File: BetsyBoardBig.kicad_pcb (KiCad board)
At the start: 4 copper layers, 50 x 50 mm, 55 parts, among them J1 USB_B_Micro, J2 Micro_SD_Card, J3 CLOCKS, J4 USART3, J5 SPI/USART, J6 I2C, J7 ANALOG, P3 CORTEX-JTAG, P6 BATT, Q1 BSS138BKS, SW1 JUMPER_x2, SW2 RST, SW3 USR, U1 TLV75733PDBVR‎, U2 USBLC6-2SC6, U3 APX823, U4 STM32L486Rx-LQFP64, U5 IS25WP256D-xM, U6 74LVC1G3157, X1 XTAL, Y1 Crystal

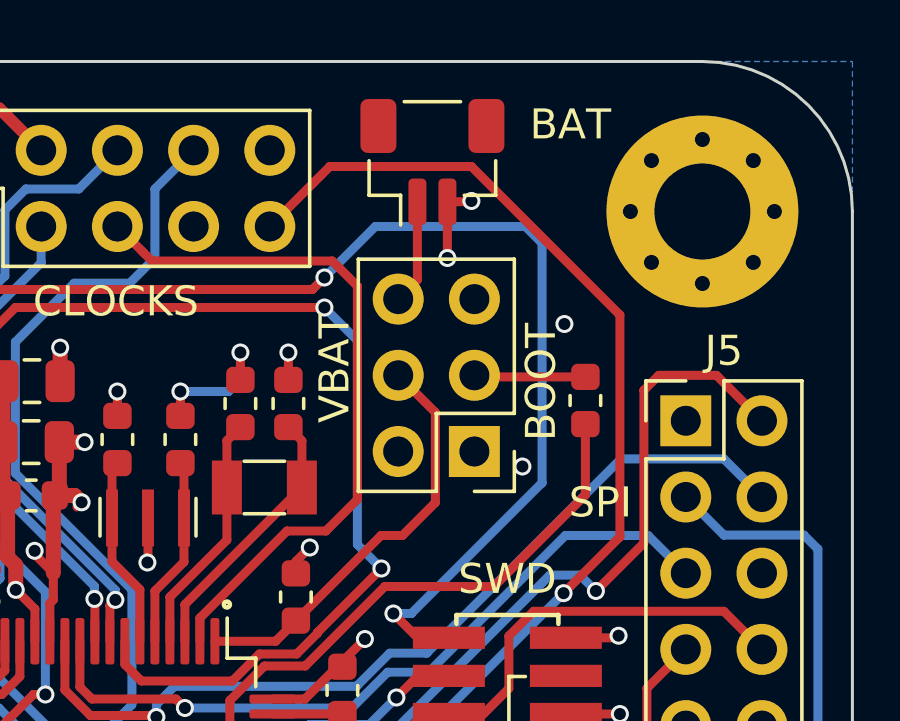
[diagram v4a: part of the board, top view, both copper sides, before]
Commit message: Use a battery header I can actually procure.
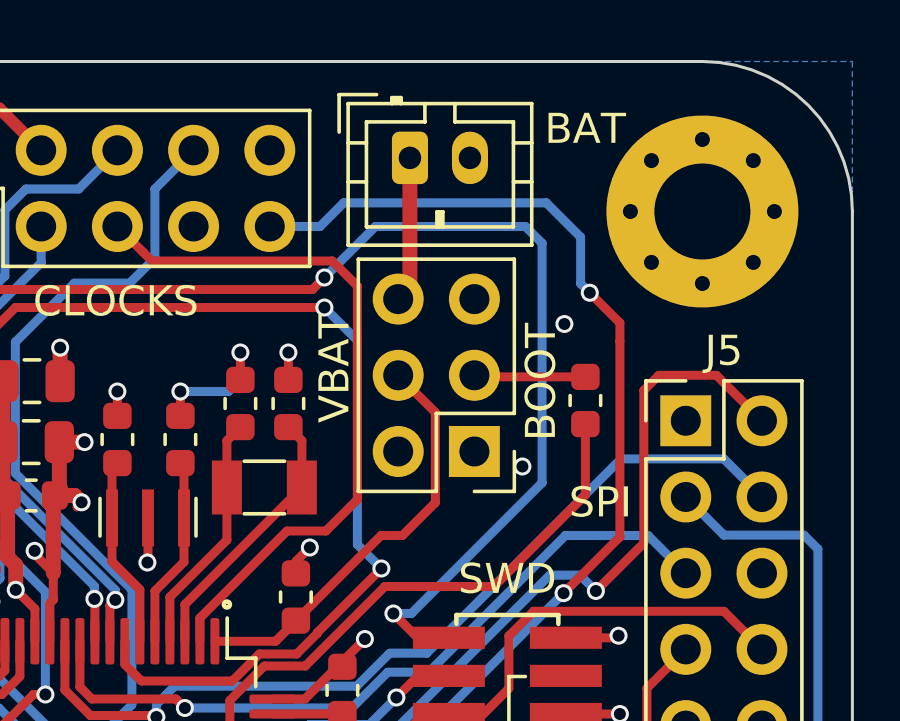
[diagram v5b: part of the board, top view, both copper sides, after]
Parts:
- P6: footprint Connector_JST:JST_SH_BM02B-SRSS-TB_1x02-1MP_P1.00mm_Vertical -> Connector_JST:JST_PH_B2B-PH-K_1x02_P2.00mm_Vertical
- moved P6 0.76 mm to (130.3, 53.2)
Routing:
- net GND: track 93.2 -> 90.5 mm, vias 48 -> 46
- net /VBAT_IN: track 3.51 -> 4.87 mm
- net /SWCLK_JTCK: track 43.3 -> 43.0 mm, vias 3 -> 4

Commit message: Simplify a bit.
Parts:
- J3: footprint Connector_PinHeader_2.54mm:PinHeader_2x05_P2.54mm_Vertical -> Connector_PinHeader_2.54mm:PinHeader_2x04_P2.54mm_Vertical
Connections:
- J3 pad 2: /EXTSCL -> /OCLK_LS
- J3 pad 3: /RTC_OUT -> /EXTSCL
- J3 pad 4: /EXTSDA -> /OCLK_M
- J3 pad 5: /RTC_TS -> /EXTSDA
- J3 pad 6: /OCLK_LS -> /RTC_OUT
- J3 pad 7: (no net) -> GND
- J3 pad 8: /OCLK_M -> /RTC_TS
- J5 pad 7: /SWDIO_JTMS -> (no net)
- J5 pad 8: /SWO_JTDO -> (no net)
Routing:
- net /SWCLK_JTCK: track 43.0 -> 19.5 mm, vias 4 -> 3
- net /SWDIO_JTMS: track 28.6 -> 12.1 mm
- net /SWO_JTDO: track 21.3 -> 7.92 mm
- net /QSPI_IO3: track 26.7 -> 14.2 mm
- net /RTC_OUT: track 29.4 -> 39.2 mm
- net /SDMMC_CLK: track 30.4 -> 20.7 mm, vias 0 -> 2
- net /SDMMC_D2: track 30.6 -> 21.9 mm
- net /SDMMC_CMD: track 30.5 -> 23.0 mm, vias 0 -> 2
- net /SDMMC_D3: track 30.4 -> 23.0 mm
- net VCC: track 70.4 -> 75.1 mm, vias 23 -> 22
- net /LED_RED: track 23.5 -> 20.2 mm
- net /OCLK_M: track 35.5 -> 32.7 mm
- net /USR_BTN: track 35.6 -> 33.1 mm
- net /OCLK_LS: track 22.6 -> 20.6 mm
- net /USART3_TXD: track 26.4 -> 24.5 mm
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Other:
- board text added: "JLCJLCJLCJLC"

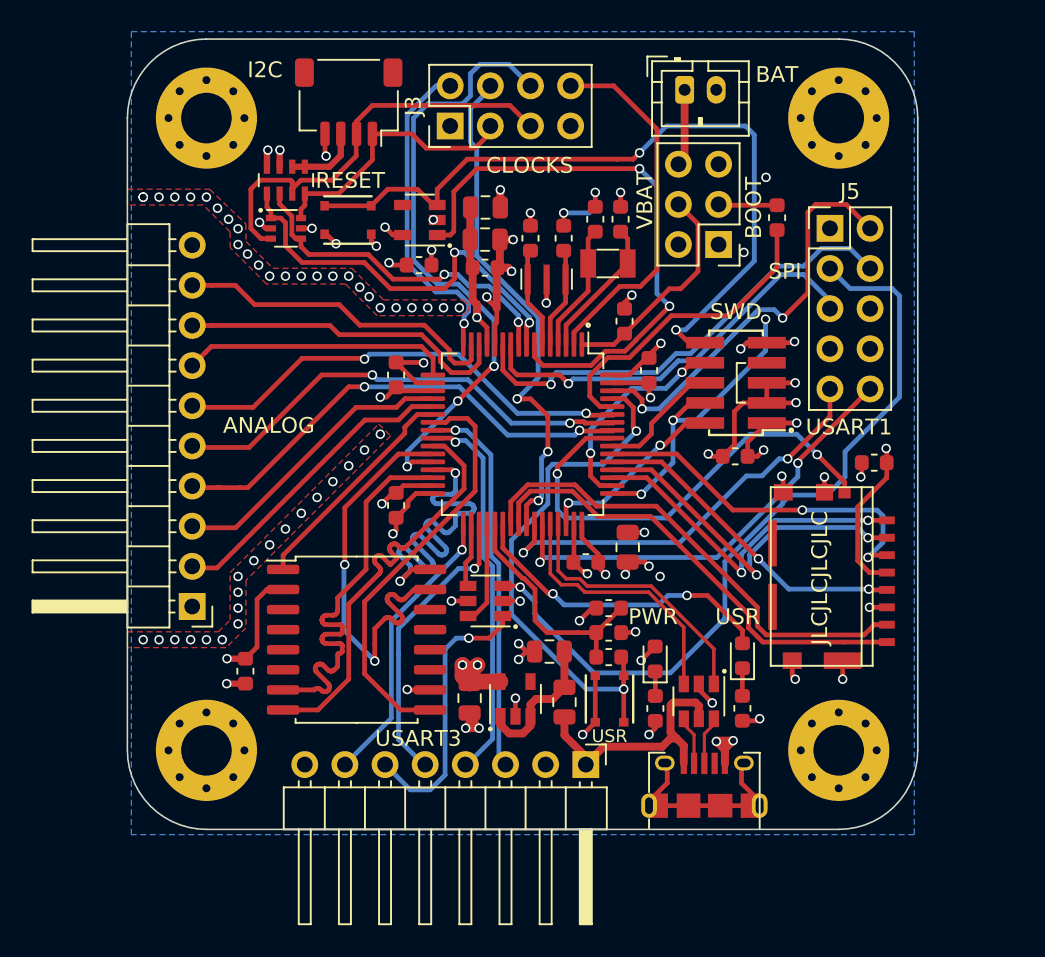
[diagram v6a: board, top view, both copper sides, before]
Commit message: Fitting in bigger buttons and adding reset/boot circuit.
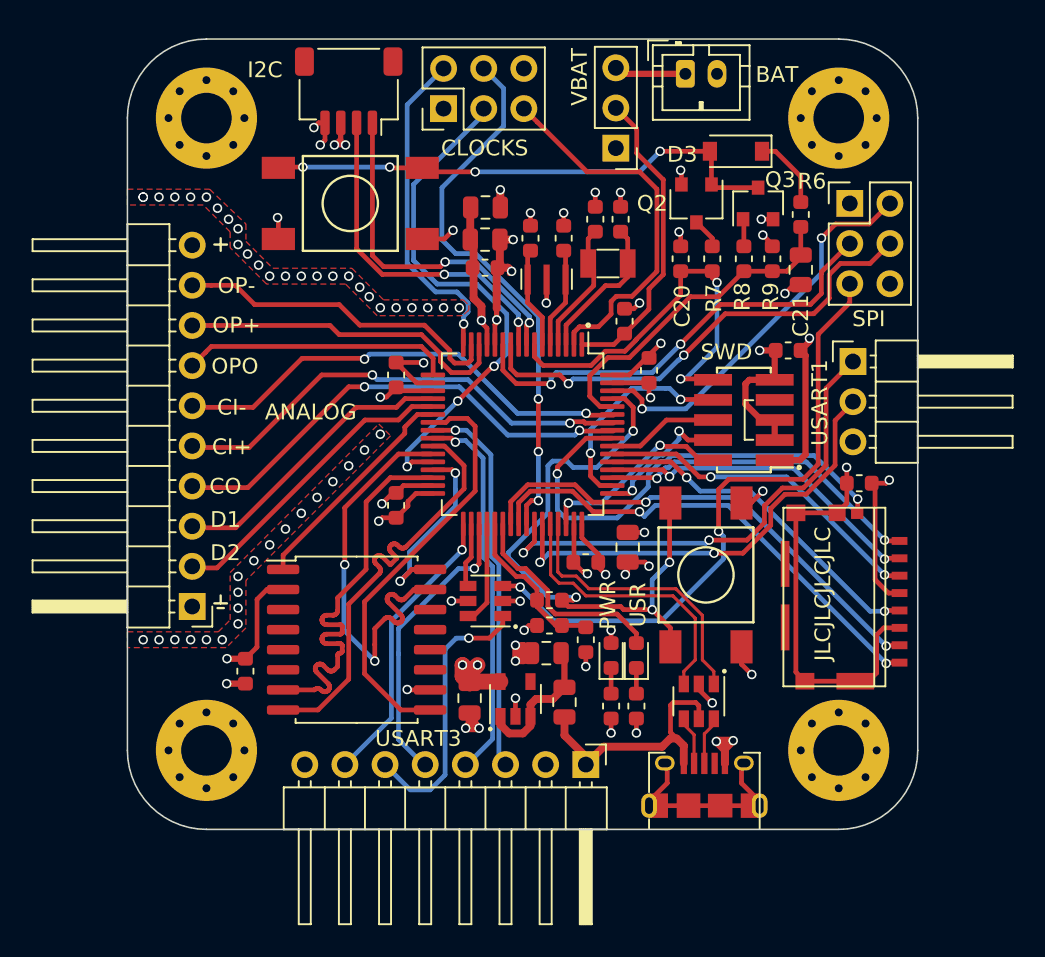
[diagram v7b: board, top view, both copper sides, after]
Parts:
- removed C7: 0.1uF, Capacitor_SMD:C_0603_1608Metric
- removed Q1: BSS138BKS, Package_TO_SOT_SMD:SOT-363_SC-70-6
- removed R2: 10k, Resistor_SMD:R_0603_1608Metric
- removed RN1: 10K, Resistor_SMD:R_Array_Concave_4x0603
- removed SW2: RST, engstad:tactile-switch-evpay-34x29mm
- removed SW3: USR, engstad:tactile-switch-evpay-34x29mm
- removed U3: APX823, Package_TO_SOT_SMD:SOT-23-5
- added C20: 0.1uF, Capacitor_SMD:C_0603_1608Metric, F.Cu at (130.0, 63.9)
- added C21: 10uF/5%, Capacitor_SMD:C_0805_2012Metric, F.Cu at (137.6, 64.6)
- added D3: 1N4148W, Diode_SMD:D_SOD-123, F.Cu at (133.5, 57.1)
- added J8: SPI, Connector_PinHeader_2.54mm:PinHeader_2x03_P2.54mm_Vertical, F.Cu at (140.7, 60.4)
- added Q2: DTC123JKA, Package_TO_SOT_SMD:SC-59, F.Cu at (131.0, 60.4)
- added Q3: MMBFJ270, Package_TO_SOT_SMD:SOT-23, F.Cu at (134.9, 60.4)
- added R6: 330K, Resistor_SMD:R_0603_1608Metric, F.Cu at (137.6, 61.1)
- added R7: 100R, Resistor_SMD:R_0603_1608Metric, F.Cu at (132.0, 63.9)
- added R8: 10K, Resistor_SMD:R_0603_1608Metric, F.Cu at (134.0, 63.9)
- added R9: 1M, Resistor_SMD:R_0603_1608Metric, F.Cu at (135.8, 63.9)
- added SW4: JUMPER, Connector_PinHeader_2.54mm:PinHeader_1x03_P2.54mm_Vertical, F.Cu at (125.9, 56.9)
- added SW5: SW_PUSH_NO_ALT, engstad:TACTILE_SWITCH-TE-FSM4JSMAATR, F.Cu at (109.1, 60.4)
- J3: footprint Connector_PinHeader_2.54mm:PinHeader_2x04_P2.54mm_Vertical -> Connector_PinHeader_2.54mm:PinHeader_2x03_P2.54mm_Vertical
- J5: value SPI/USART -> USART1; footprint Connector_PinHeader_2.54mm:PinHeader_2x05_P2.54mm_Vertical -> Connector_PinHeader_2.54mm:PinHeader_1x03_P2.54mm_Horizontal
- SW1: value JUMPER_x2 -> SW_PUSH_NO_ALT; footprint Connector_PinHeader_2.54mm:PinHeader_2x03_P2.54mm_Vertical -> engstad:TACTILE_SWITCH-TE-FSM4JSMAATR
- moved SW1 20.9 mm to (131.6, 83.9), turned to 270 degrees
- moved J5 8.55 mm to (140.9, 70.4)
- moved C3 7.49 mm to (136.8, 69.7)
- moved D1 6.71 mm to (127.2, 89.0)
- moved R3 6.71 mm to (127.2, 92.2)
- moved R1 5.20 mm to (121.7, 85.5)
- moved R5 3.91 mm to (121.7, 87.1)
- moved R4 2.80 mm to (125.6, 92.2)
- moved D2 2.79 mm to (125.6, 89.0)
- moved P3 2.40 mm to (134.0, 74.1)
- moved C11 1.61 mm to (141.3, 78.1)
- moved J2 1.53 mm to (140.3, 85.3)
- moved C4 1.52 mm to (124.0, 88.0), turned to 270 degrees
- moved J3 1.18 mm to (115.0, 54.4)
- moved P6 1.01 mm to (130.3, 52.2)
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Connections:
- net /OTG_FS_D+ renamed /OTGFS_D+
- net /OTG_FS_D- renamed /OTGFS_D-
- J3 pad 3: /EXTSCL -> /RTC_OUT
- J3 pad 5: /EXTSDA -> /RTC_TS
- J3 pad 6: /RTC_OUT -> GND
- J5 pad 1: VCC -> /USART1_TX
- J5 pad 2: /SPI2_SS# -> /USART1_RX
- J5 pad 3: /SPI2_SCK -> GND
- J6 pad 1: /EXTSCL -> /I2C_SCL
- J6 pad 2: /EXTSDA -> /I2C_SDA
- J6 pad 3: +5V -> VCC
- P3 pad 10: /RSTIN# -> /~RST
- SW1 pad 1: VCC -> GND
- SW1 pad 2: VCC -> /USR_BTN
- U4 pad 10: /SPI2_MISO -> /SPI2_CIPO
- U4 pad 11: /SPI2_MOSI -> /SPI2_COPI
- U4 pad 62: /SPI2_SS# -> /SPI2_CS#
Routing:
- net /RSTIN#: track 47.9 -> 0.00 mm, vias 2 -> 0
- net /RSTBTN: track 0.00 -> 33.2 mm, vias 0 -> 4
- net /SPI2_CIPO: track 0.00 -> 30.8 mm, vias 0 -> 2
- net /SPI2_MOSI: track 29.6 -> 0.00 mm, vias 1 -> 0
- net /SPI2_COPI: track 0.00 -> 28.7 mm, vias 0 -> 2
- net /EXTSDA: track 27.0 -> 0.00 mm
- net /SPI2_SS#: track 26.5 -> 0.00 mm, vias 2 -> 0
- net /SPI2_MISO: track 26.2 -> 0.00 mm, vias 1 -> 0
- net /SPI2_CS#: track 0.00 -> 25.1 mm, vias 0 -> 2
- net GND: track 90.6 -> 108.4 mm, vias 47 -> 38
- net /EXTSCL: track 17.1 -> 0.00 mm
- net /QSPI_SCK: track 26.7 -> 12.0 mm
- net /~RST: track 36.6 -> 25.8 mm
- net /SWCLK_JTCK: track 19.5 -> 8.90 mm, vias 3 -> 2
- net /SPI2_SCK: track 49.7 -> 40.3 mm, vias 1 -> 2
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- removed copper zone on B.Cu, net GND
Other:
- board text added: "CI+"
- board text added: "CI-"
- board text added: "CO"
- board text added: "D1"
- board text added: "D2"
- board text added: "OP+"
- board text added: "OP-"
- board text added: "OPO"
- board text removed: "BOOT"
- board text removed: "RESET"

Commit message: Additions due to single-button boot logic.
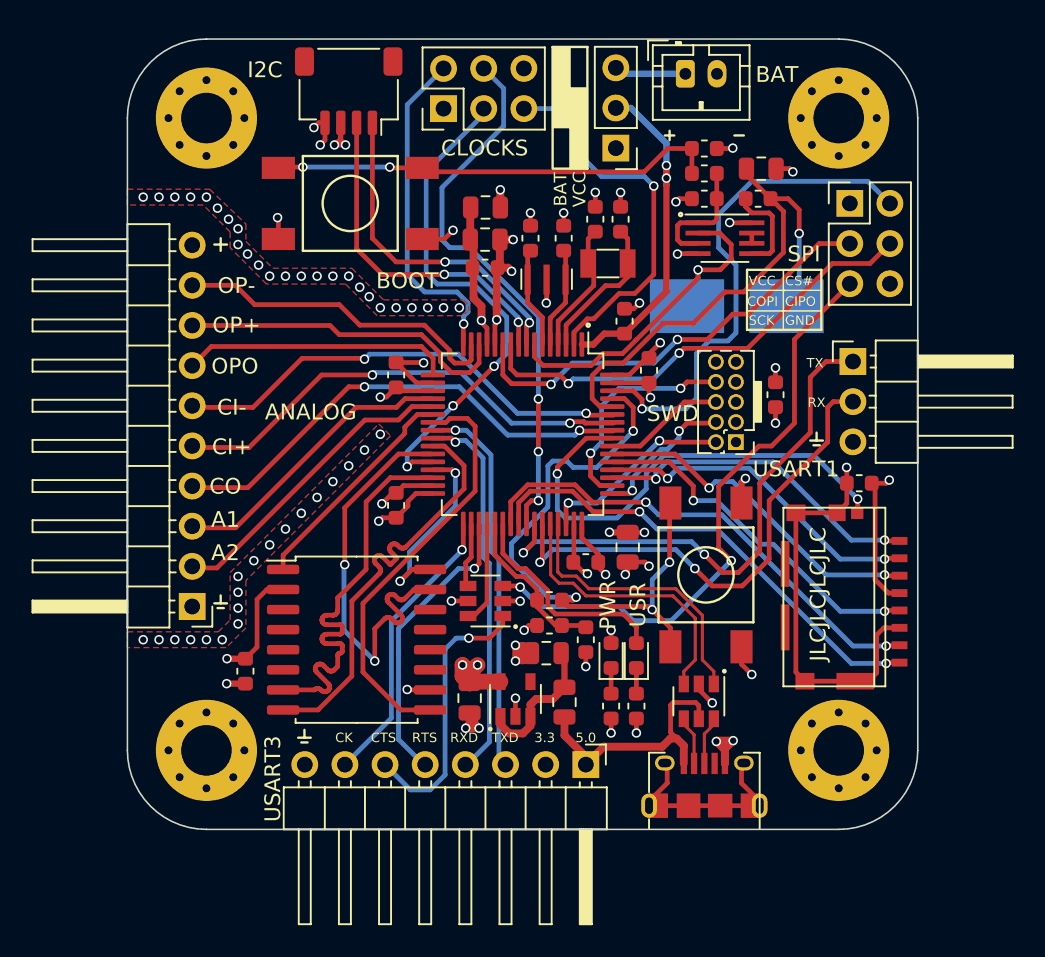
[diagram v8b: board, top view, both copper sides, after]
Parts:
- removed the C20 at (130.0, 63.9)
- removed C21: 10uF/5%, Capacitor_SMD:C_0805_2012Metric
- removed D3: 1N4148W, Diode_SMD:D_SOD-123
- removed Q2: DTC123JKA, Package_TO_SOT_SMD:SC-59
- removed Q3: MMBFJ270, Package_TO_SOT_SMD:SOT-23
- removed the R6 at (137.6, 61.1)
- removed the R7 at (132.0, 63.9)
- removed R8: 10K, Resistor_SMD:R_0603_1608Metric
- removed R9: 1M, Resistor_SMD:R_0603_1608Metric
- added C11: 0.1uF, Capacitor_SMD:C_0603_1608Metric, F.Cu at (131.5, 60.1)
- added C12: 10uF, Capacitor_SMD:C_0805_2012Metric, F.Cu at (135.1, 58.2)
- added R1: 10K, Resistor_SMD:R_0603_1608Metric, F.Cu at (131.5, 56.9)
- added R2: 1K, Resistor_SMD:R_0603_1608Metric, F.Cu at (131.5, 58.5)
- added R3: 100K, Resistor_SMD:R_0603_1608Metric, F.Cu at (134.9, 60.1)
- added TP1-RST#1: TestPoint_Probe, engstad:test-point-smd-5016, B.Cu at (130.4, 66.9)
- added TP2-BOOT0: TestPoint_Probe, engstad:test-point-smd-5016, B.Cu at (136.7, 66.9)
- added U3: 74LVC3G14, Package_SO:SSOP-8_2.95x2.8mm_P0.65mm, F.Cu at (132.8, 62.6)
- P2: renamed from P3; footprint engstad:conn-jtag-0.05 -> Connector_PinHeader_1.27mm:PinHeader_2x05_P1.27mm_Vertical
- SW2: renamed from SW5; value SW_PUSH_NO_ALT -> TE-FSM4J
- moved C1 2.91 mm to (136.0, 72.5), turned to 90 degrees
- moved P2 1.49 mm to (133.5, 75.5), turned to 180 degrees
- renumbered C3 to C1, C9 to C10, C4 to C13, C11 to C14, C12 to C15, C14 to C16, C15 to C17, C16 to C18, C17 to C19, C10 to C2, C19 to C20, C1 to C3, C2 to C4, C13 to C7, C18 to C8, C8 to C9, J3 to J1, J8 to J2, J1 to J3, J5 to J4, J6 to J5, J4 to J6, J2 to J8, P6 to P1, R5 to R4, R1 to R5, R3 to R6, R4 to R7, SW4 to SW1, SW1 to SW3, U6 to U5, U5 to U6
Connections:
- P2 pad 10: /~RST -> (no net)
- SW2 pad 1: VCC -> GND
- SW2 pad 2: /RSTBTN -> Net-(R1-Pad2)
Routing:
- net /RSTBTN: track 33.2 -> 0.00 mm, vias 4 -> 0
- net Net-(R1-Pad2): track 0.00 -> 28.5 mm, vias 0 -> 2
- net /BOOT0: track 21.0 -> 32.7 mm, vias 0 -> 1
- net VCC: track 77.9 -> 68.0 mm
- net /~MR: track 0.00 -> 7.85 mm
- net /SPI2_CS#: track 25.1 -> 32.5 mm, vias 2 -> 1
- net Net-(R3-Pad2): track 0.00 -> 6.02 mm
- net GND: track 108.4 -> 102.8 mm, vias 38 -> 39
- net Net-(D3-Pad1): track 4.73 -> 0.00 mm
- net /~RST: track 25.8 -> 22.3 mm, vias 2 -> 1
- net /USART1_RX: track 28.8 -> 31.9 mm
- net /USART1_TX: track 31.5 -> 34.2 mm
- net Net-(Q2-Pad3): track 1.93 -> 0.00 mm
- net Net-(Q3-Pad1): track 1.73 -> 0.00 mm
- net /VBAT: track 19.5 -> 21.0 mm, vias 0 -> 2
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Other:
- board text added: "3.3"
- board text added: "5.0"
- board text added: "A1"
- board text added: "A2"
- board text added: "AGND"
- board text added: "BOOT"
- board text added: "BOOT0"
- board text added: "CIPO"
- board text added: "CK"
- board text added: "COPI"
- board text added: "CS#"
- board text added: "CTS"
- board text added: "GND"
- board text added: "OCLK_LS"
- board text added: "OCLK_M"
- board text added: "PA0/ADC5"
- board text added: "PA1/ADC6"
- board text added: "PA10"
- board text added: "PA3/ADC8"
- board text added: "PA4/ADC9"
- board text added: "PA5/ADC10"
- board text added: "PA9"
- board text added: "PB12"
- board text added: "PB13 *"
- board text added: "PB14"
- board text added: "PB5"
- board text added: "PB6"
- board text added: "PB7"
- board text added: "PB8"
- board text added: "PB9"
- board text added: "PC2"
- board text added: "PC3"
- board text added: "PC4/CMP1_IN-/A13"
- board text added: "PC5/CMP1_IN-/A14"
- board text added: "RTC_OUT"
- board text added: "RTC_TS"
- board text added: "RTS"
- board text added: "RX"
- board text added: "RXD"
- board text added: "SCK"
- board text added: "TX"
- board text added: "TXD"
- board text added: "VBUS (5V)"
- board text added: "VCC"
- board text added: "VCC (3.3V)"
- board text added: "VCCA"
- board text added: "~RST~"
- board text removed: "D1"
- board text removed: "D2"
- board text removed: "VBAT"
